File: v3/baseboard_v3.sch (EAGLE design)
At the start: 40 parts, among them Q1 18A/40V/5mΩ, U1 MC33926, U2 MC33926

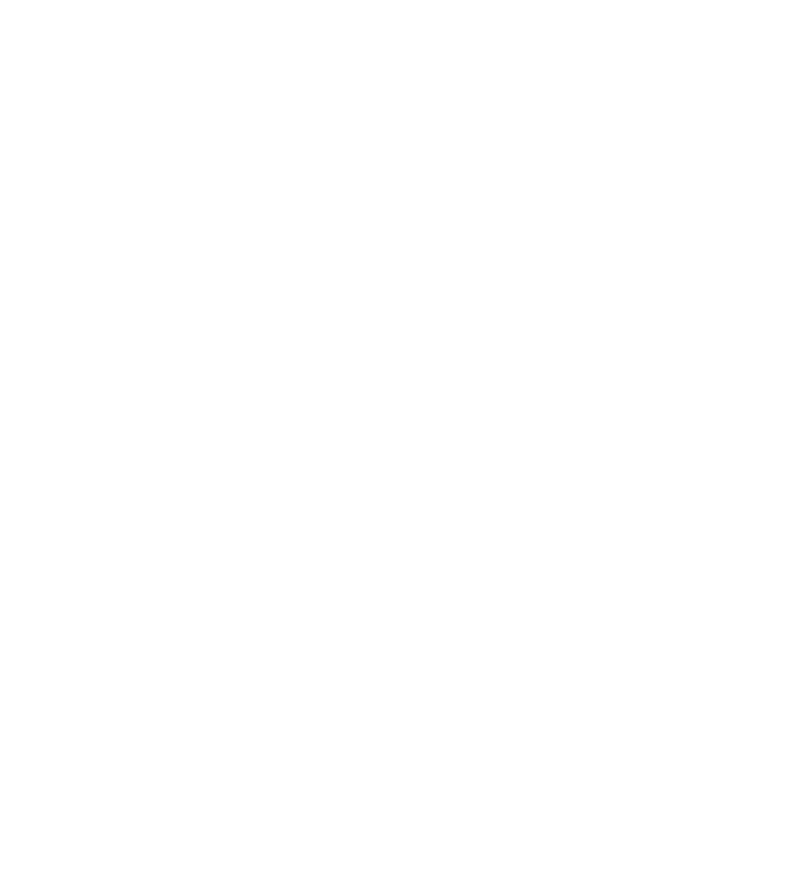
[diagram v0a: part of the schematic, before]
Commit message: Adding progress on designing powerboard.
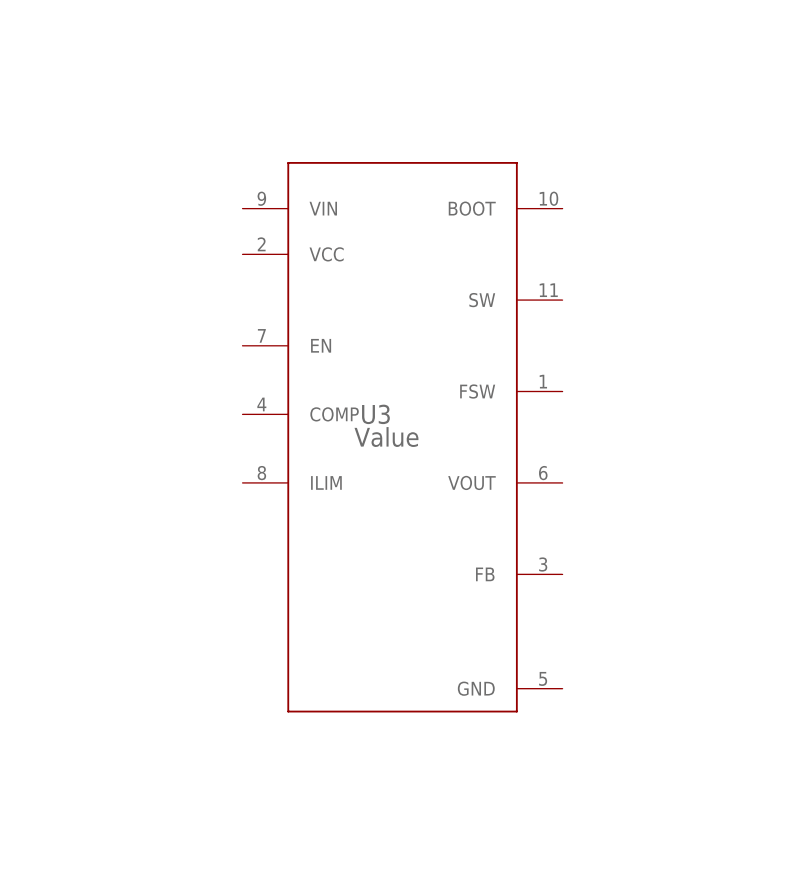
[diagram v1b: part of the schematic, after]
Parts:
- added U3: Value, powerbench:TPS61089RNRR
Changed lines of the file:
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@@
 <part name="C6" library="SparkFun-Capacitors" deviceset="0.1UF" device="-0603-25V-(+80/-20%)" value="0.1uF"/>
 <part name="SUPPLY18" library="SparkFun-PowerSymbols" deviceset="AGND" device=""/>
+<part name="U3" library="powerbench" deviceset="TPS61089RNRR" device="" value="Value"/>
 </parts>
 <sheets>
@@
 </instance>
 <instance part="SUPPLY18" gate="G$1" x="220.98" y="215.9"/>
+<instance part="U3" gate="A" x="279.4" y="175.26"/>
 </instances>
 <busses>

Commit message: Moving away from bb ideas.
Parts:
- removed U3: Value, powerbench:TPS61089RNRR
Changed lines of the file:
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@@
 <?xml version="1.0" encoding="utf-8"?>
 <!DOCTYPE eagle SYSTEM "eagle.dtd">
-<eagle version="8.0.1">
+<eagle version="8.1.0">
 <drawing>
 <settings>
@@
 <part name="C6" library="SparkFun-Capacitors" deviceset="0.1UF" device="-0603-25V-(+80/-20%)" value="0.1uF"/>
 <part name="SUPPLY18" library="SparkFun-PowerSymbols" deviceset="AGND" device=""/>
-<part name="U3" library="powerbench" deviceset="TPS61089RNRR" device="" value="Value"/>
 </parts>
 <sheets>
@@
 </instance>
 <instance part="SUPPLY18" gate="G$1" x="220.98" y="215.9"/>
-<instance part="U3" gate="A" x="279.4" y="175.26"/>
 </instances>
 <busses>
